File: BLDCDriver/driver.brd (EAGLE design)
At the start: 68 parts, among them CON1 XT30PW-M, Q1 NJM7800S, Q2 SIZ240DT-T1-GE3, Q3 SIZ240DT-T1-GE3, Q4 SIZ240DT-T1-GE3, U1 QFN50P400X400X100-25NDRV8300D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, U2 AS5048A-HTSP-500, U4 SOP80P620X125-8N

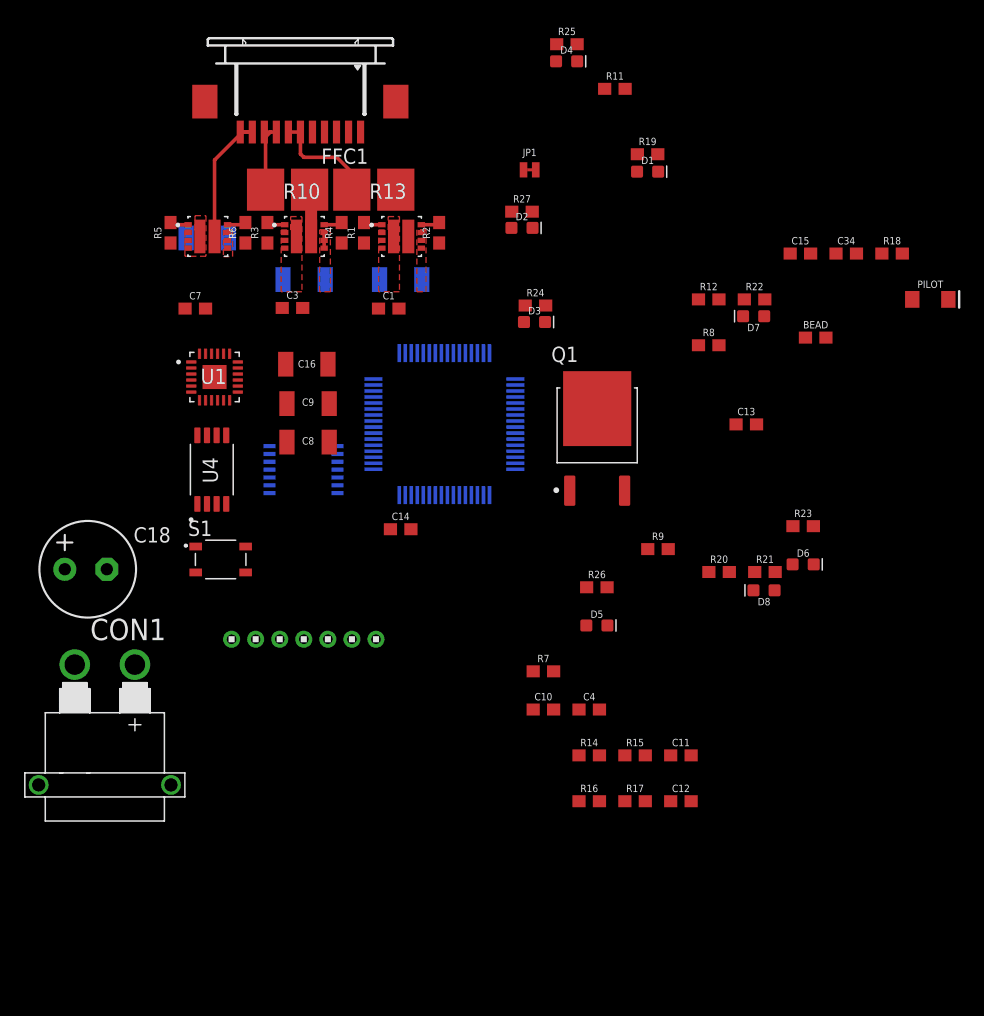
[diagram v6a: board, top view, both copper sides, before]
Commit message: モータ固定台のシルク入れた
# ==== Emojis ====
# ✨ :sparkles: Add new feature
# ✅  :white_check_mark: Update existing feature (not bug)
# ⚠️  :warning: Fix bug/error
# 🔥  :fire: Remove files or features
# ✏️ :pencil2: Fix typos
# 📝  :memo: Update documentation
# ♻️  :recycle: Dependencies update
# 🐧  :penguin: Improved the Linux
# 🍎  :apple: Improved the macOS
# 🔖 :bookmark: Add new library
# 🎉  :tada: Initial commit

# ==== Format ====
# :emoji: Subject
#
# Commit body...

# ==== Messages ====
# 新規(ファイル)機能追加: Add
# 機能修正、既存機能追加（バグではない): Update
# リファクタリング: Clean
# ファイル名変更:
# 削除など: Remove
# バグ修正: Fix
# バージョンアップ: Upgrade
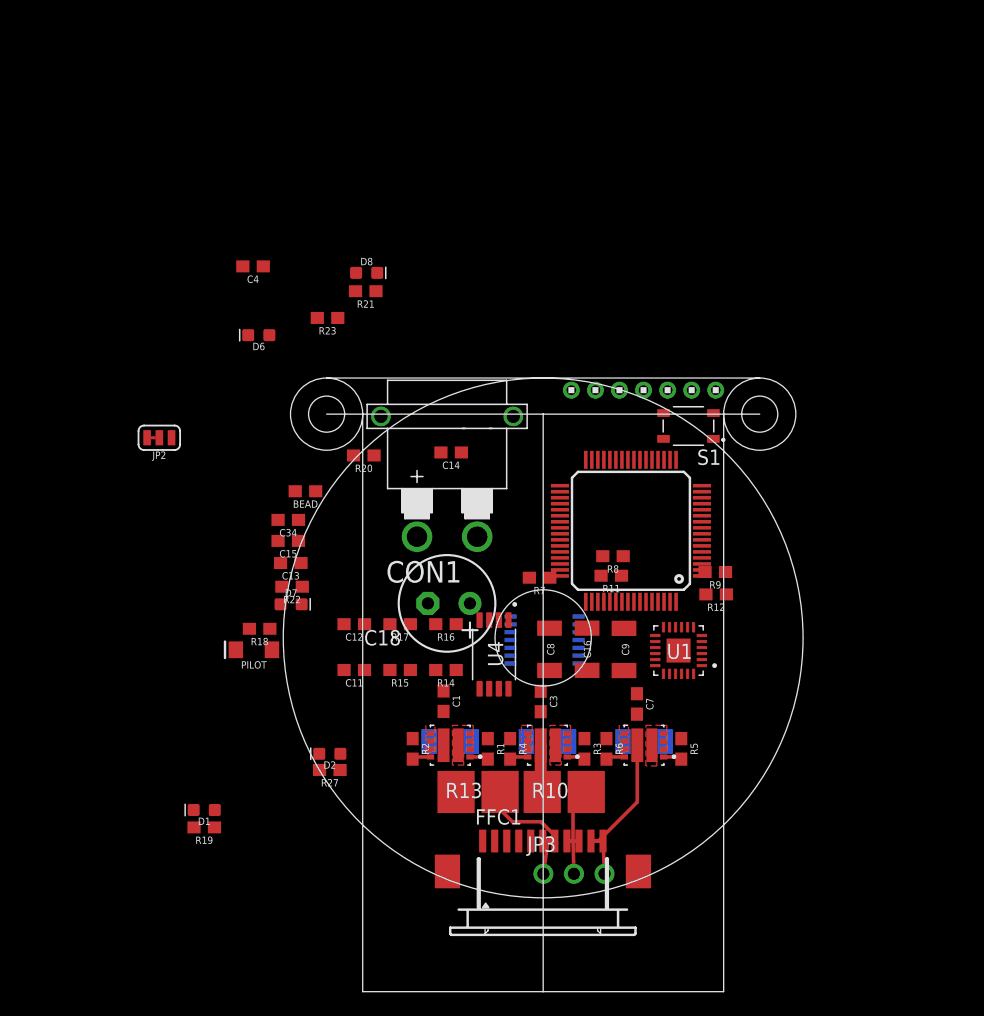
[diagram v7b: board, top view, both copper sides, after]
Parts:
- removed C10: 0.1uF, SparkFun-Capacitors:0603
- removed D3, D4, D5: WHITE, SparkFun-LED:LED-0603
- removed JP1: JUMPER-SMT_2_NC_TRACE_NO-SILK, SparkFun-Jumpers:SMT-JUMPER_2_NC_TRACE_NO-SILK
- removed Q1: NJM7800S, NJM7800S:NJM7800S
- removed R24, R25: 10k, SparkFun-Resistors:0603
- removed R26: 7k, SparkFun-Resistors:0603
- added JP2: JUMPER-SMT_3_1-NC_TRACE_SILK, SparkFun-Jumpers:SMT-JUMPER_3_1-NC_TRACE_SILK
- added JP3: (no value), adafruit:1X03-CLEANBIG
- moved FFC1 67.0 mm to (26.6, -18.5), turned to 0 degrees
- moved R19 67.0 mm to (-1.52, -14.9), turned to 180 degrees
- moved D1 64.6 mm to (-1.52, -13.4), turned to 180 degrees
- moved PILOT 63.3 mm to (2.61, -0.11), turned to 180 degrees
- moved R18 61.1 mm to (3.09, 1.63), turned to 180 degrees
- moved R5 60.3 mm to (38.1, -8.35), turned to 270 degrees
- moved Q4 55.7 mm to (35.0, -8.05), turned to 180 degrees
- moved C6 55.4 mm to (35.0, -7.74), turned to 180 degrees
- moved R10 55.1 mm to (28.4, -11.9), turned to 0 degrees
- moved R6 52.3 mm to (31.9, -8.35), turned to 270 degrees
- moved C34 51.4 mm to (5.47, 10.7), turned to 180 degrees
- moved R13 50.8 mm to (21.2, -11.9), turned to 0 degrees
- moved R3 50.3 mm to (30.1, -8.35), turned to 270 degrees
- moved C7 49.3 mm to (34.4, -4.62), turned to 270 degrees
- moved D6 49.1 mm to (3.02, 26.0), turned to 180 degrees
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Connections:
- removed net N$16: D3.A, R24.1
- removed net N$17: D4.A, R25.1
- removed net N$18: D5.A, R26.1
- removed net N$3: JP1.2, U1.MODE
- new net GVDD_IN: JP2.1
- net GND: no longer C10.2, D3.C, D4.C, D5.C, Q1.G
- net GVDD: now also JP2.2, U1.MODE; no longer JP1.1, Q1.O
- net PVDD: now also JP2.3; no longer C10.1, Q1.I
- net U: no longer R24.2
- net U_CS: now also JP3.1
- net V: no longer R25.2
- net V_CS: now also JP3.2
- net W: now also JP3.3; no longer R26.2
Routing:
- net V_CS: track 5.96 -> 8.77 mm
- net U_CS: track 9.16 -> 11.7 mm
- net W: track 11.5 -> 13.6 mm

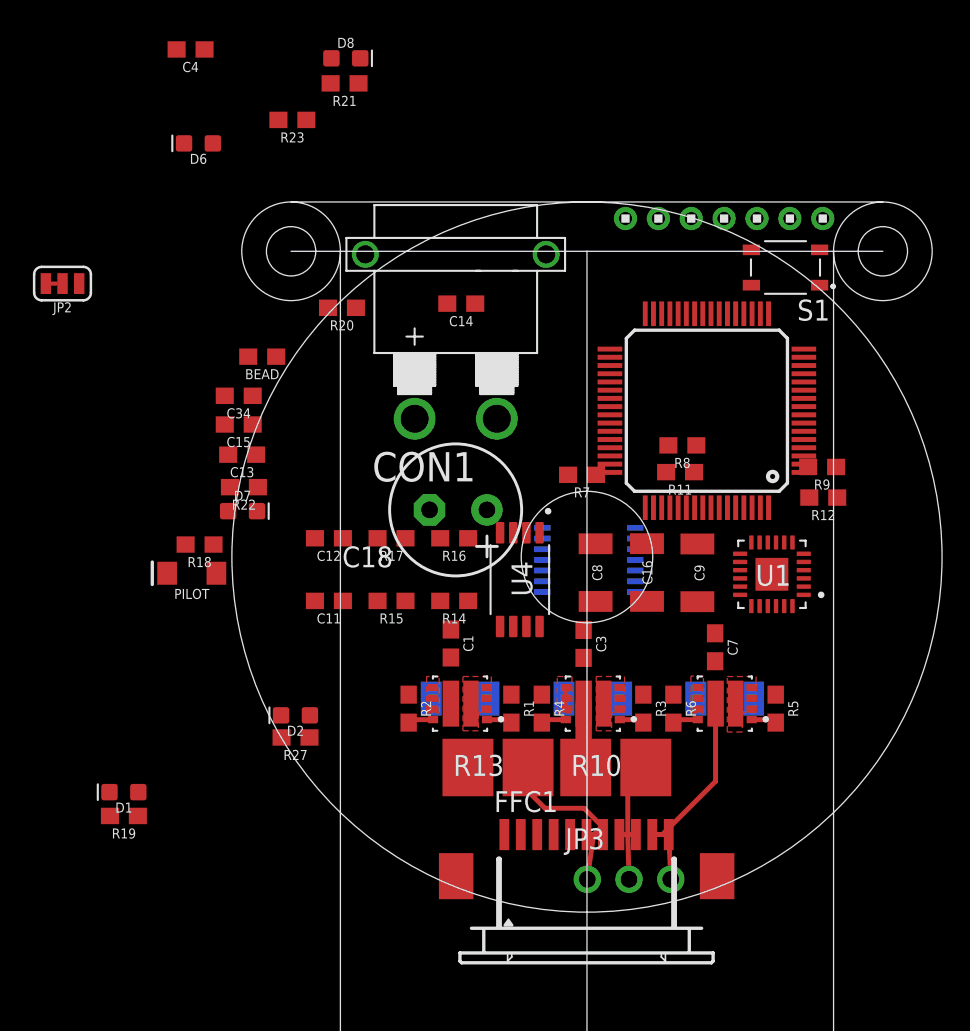
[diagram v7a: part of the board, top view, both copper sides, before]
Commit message: シャント抵抗を裏側にした。GVDD消した
# ==== Emojis ====
# ✨ :sparkles: Add new feature
# ✅  :white_check_mark: Update existing feature (not bug)
# ⚠️  :warning: Fix bug/error
# 🔥  :fire: Remove files or features
# ✏️ :pencil2: Fix typos
# 📝  :memo: Update documentation
# ♻️  :recycle: Dependencies update
# 🐧  :penguin: Improved the Linux
# 🍎  :apple: Improved the macOS
# 🔖 :bookmark: Add new library
# 🎉  :tada: Initial commit

# ==== Format ====
# :emoji: Subject
#
# Commit body...

# ==== Messages ====
# 新規(ファイル)機能追加: Add
# 機能修正、既存機能追加（バグではない): Update
# リファクタリング: Clean
# ファイル名変更:
# 削除など: Remove
# バグ修正: Fix
# バージョンアップ: Upgrade
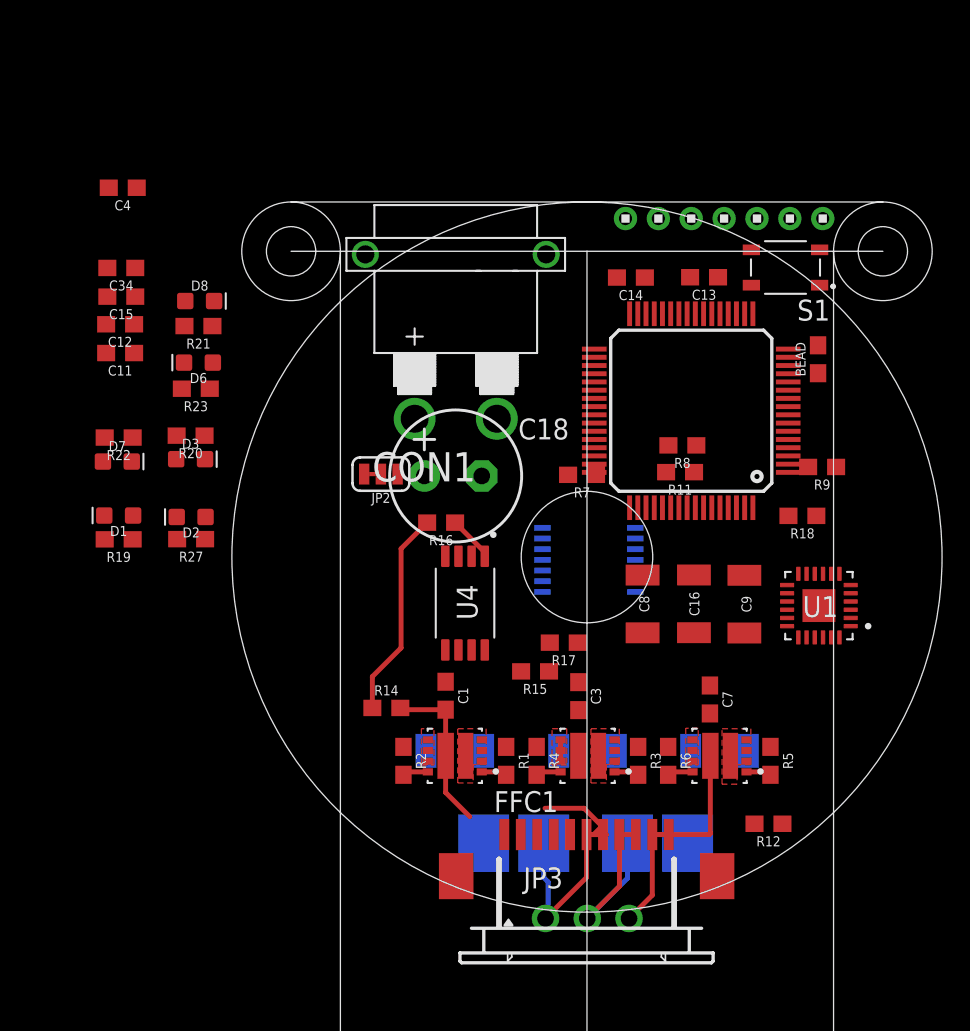
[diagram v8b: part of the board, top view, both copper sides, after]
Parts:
- removed PILOT: (no value), Custom_Designed_By_Yusei:LED-1206
- added D3: WHITE, SparkFun-LED:LED-0603
- moved R18 36.7 mm to (39.8, 3.38)
- moved BEAD 33.8 mm to (40.7, 12.9), turned to 90 degrees
- moved C13 30.1 mm to (33.8, 17.9)
- moved JP2 22.6 mm to (14.1, 5.92)
- moved R12 20.1 mm to (37.7, -15.4)
- moved C11 19.7 mm to (-1.75, 13.3)
- moved C12 18.2 mm to (-1.75, 15.0)
- moved R23 17.4 mm to (2.86, 11.1)
- moved R21 17.2 mm to (3.02, 14.9)
- moved D8 17.2 mm to (3.09, 16.4)
- moved D1 16.8 mm to (-1.84, 3.40)
- moved R19 16.8 mm to (-1.84, 1.95)
- moved R27 13.6 mm to (2.57, 1.96)
- moved D2 13.6 mm to (2.57, 3.31)
- moved D6 13.3 mm to (3.02, 12.7)
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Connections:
- net GND: now also D3.C; no longer PILOT.C
- net POWERLED_RESISTOR: now also D3.A; no longer PILOT.A
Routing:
- net N$10: track 0.00 -> 12.7 mm
- net U: track 0.00 -> 9.92 mm
- net U_CS: track 11.7 -> 17.8 mm
- net V: track 4.01 -> 0.00 mm
- net V_CS: track 8.77 -> 12.6 mm
- net C_U: track 0.00 -> 2.79 mm
- net W: track 13.6 -> 15.0 mm
